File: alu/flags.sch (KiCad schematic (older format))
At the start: 15 parts

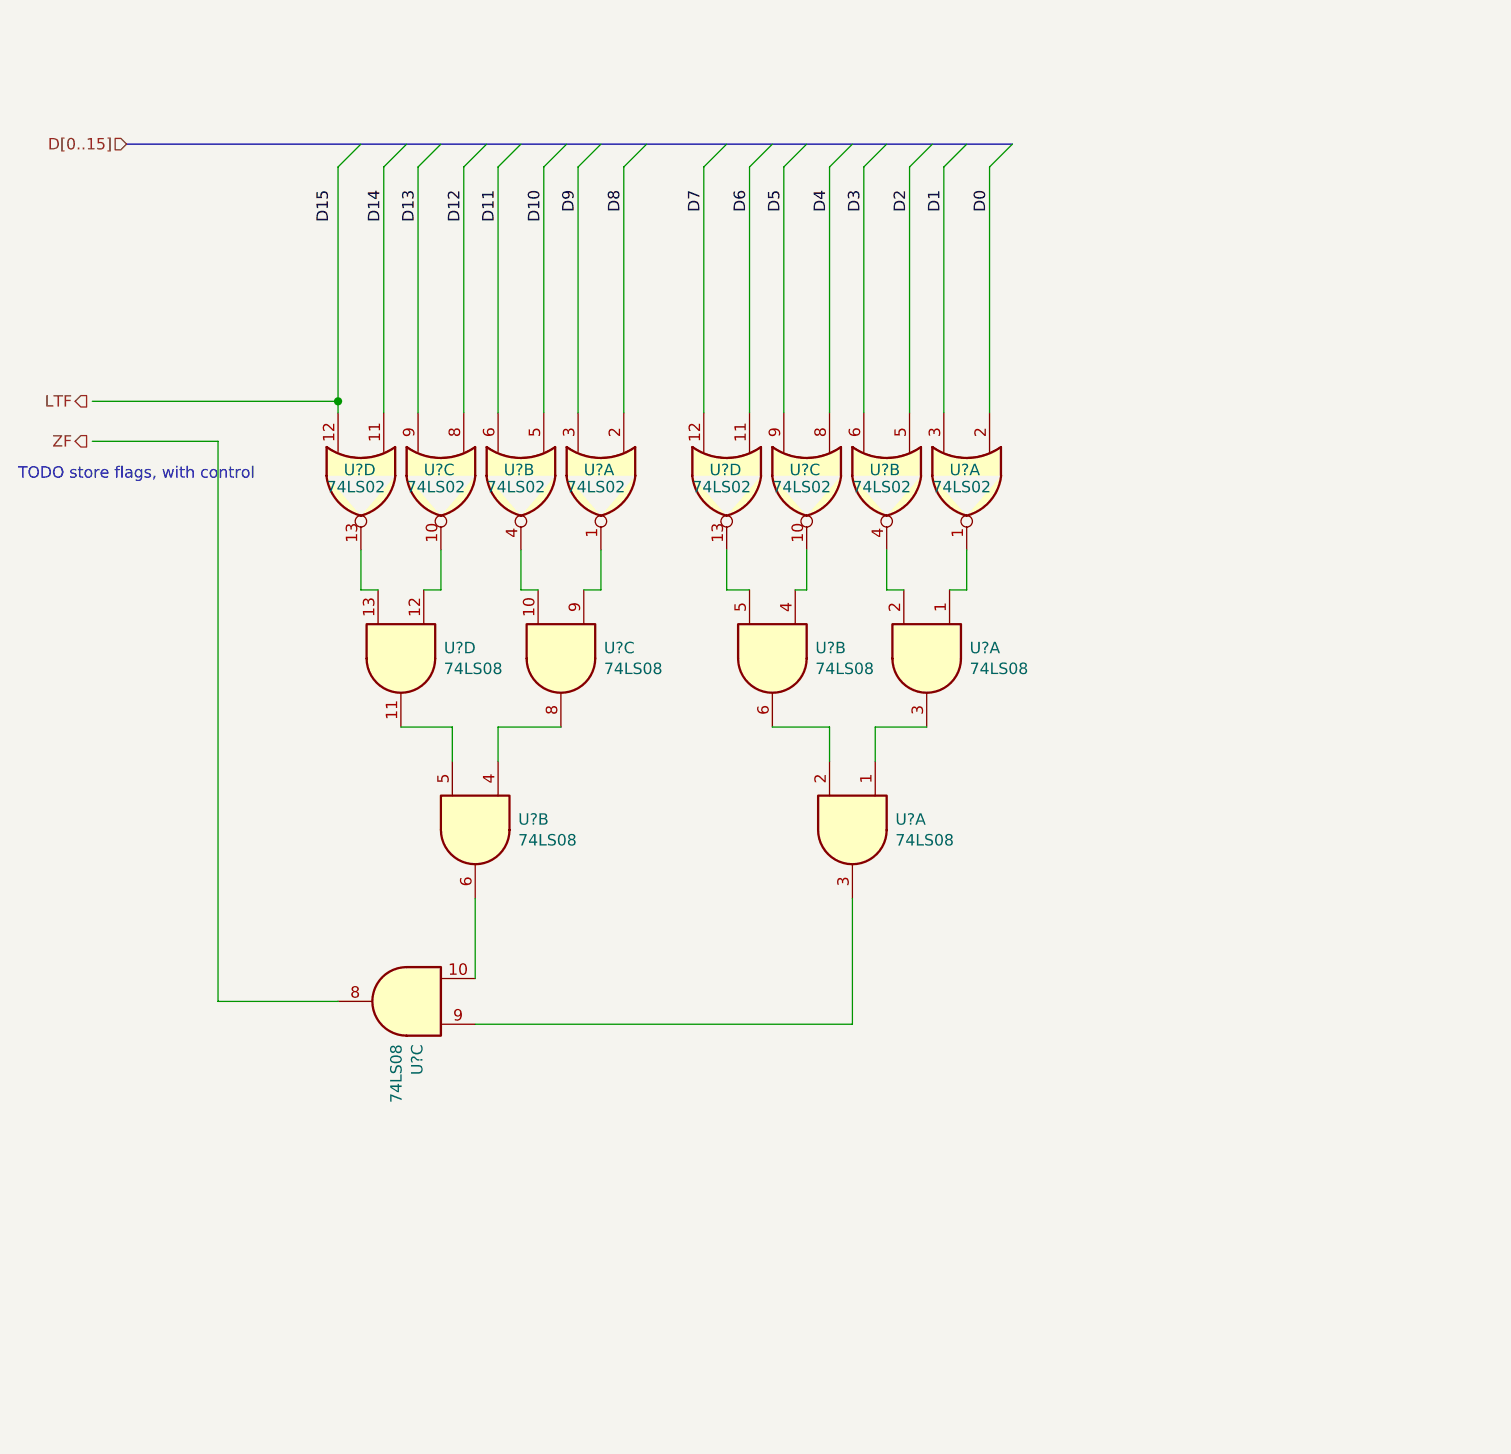
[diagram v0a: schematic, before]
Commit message: alu routed first iteration
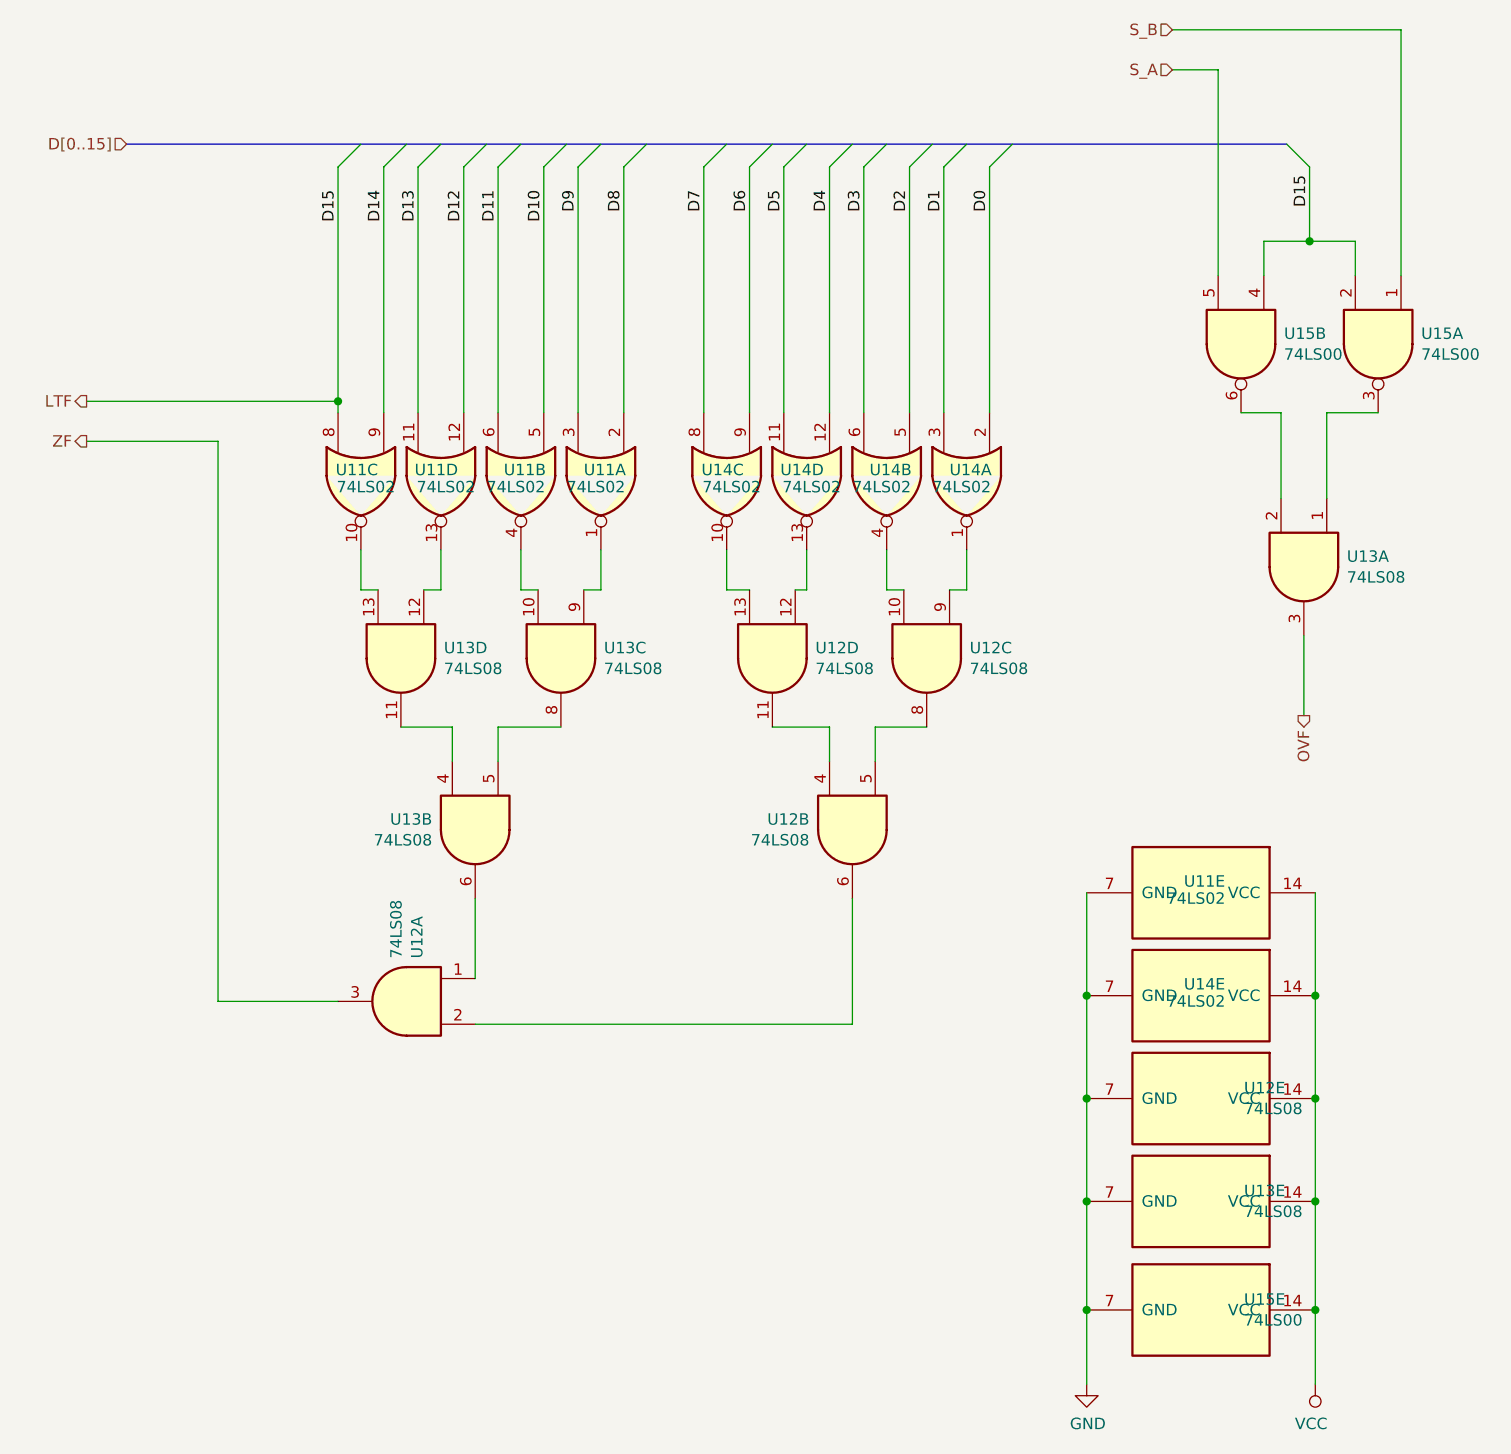
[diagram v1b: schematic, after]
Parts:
- added unit 5 of U11
- added unit 5 of U12
- added unit 1 of U13
- added unit 5 of U13
- added unit 5 of U14
- added U15: 74LS00, Package_DIP:DIP-14_W7.62mm_LongPads, symbol 74xx:74LS00
- U11, U12, U13, U14: renamed from U?; footprint (none) -> Package_DIP:DIP-14_W7.62mm_LongPads
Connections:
- net labels added: GND, OVF, S_A, S_B, VCC
- wire segments 48 -> 72
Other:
- note removed: "TODO store flags, with control"
